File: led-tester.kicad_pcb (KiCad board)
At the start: 2 copper layers, 60.2 x 87.2 mm, 41 parts, among them J1 V_In, SW1 PWR_SW

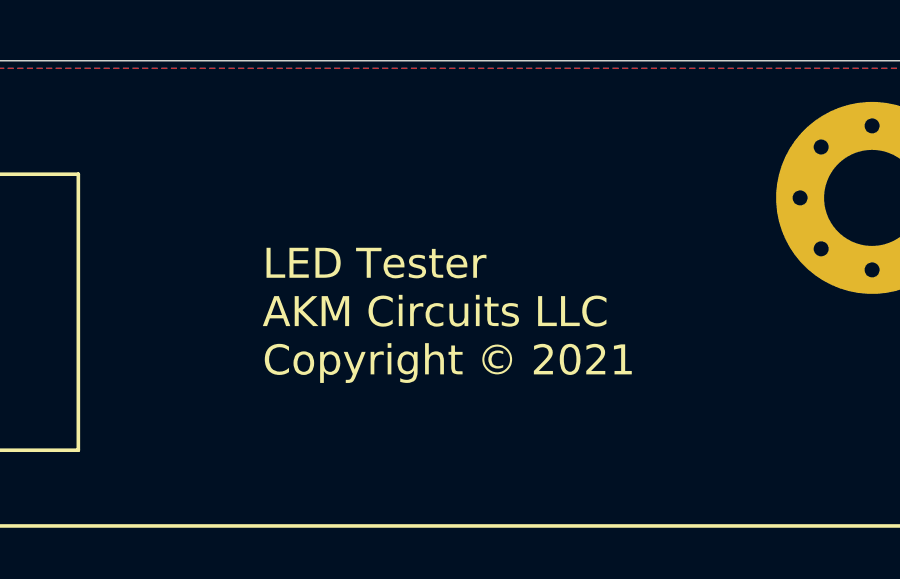
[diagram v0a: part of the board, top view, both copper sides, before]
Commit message: add revision information to silkscreen
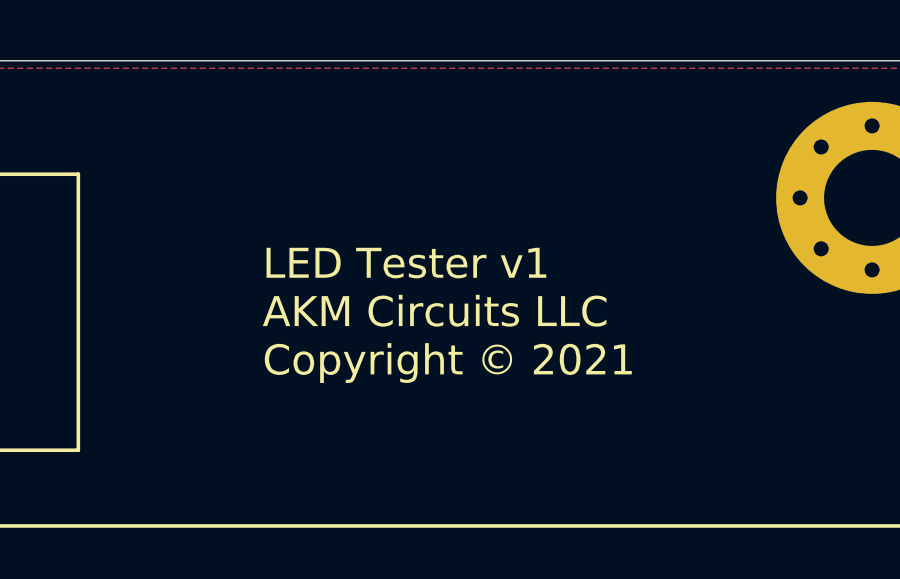
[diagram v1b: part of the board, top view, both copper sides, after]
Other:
- board text added: "LED Tester v1 AKM Circuits LLC Copyright © 2021"
- board text removed: "LED Tester AKM Circuits LLC Copyright © 2021"
